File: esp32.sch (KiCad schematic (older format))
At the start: 41 parts, among them J1 Micro_SD_Card, J10 Conn_01x01, J11 Conn_01x04, J12 Conn_01x01, J13 Conn_01x01, J14 Conn_01x01, J15 Conn_01x01, J18 Conn_01x02, J2 Conn_01x06, J25 Conn_01x01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

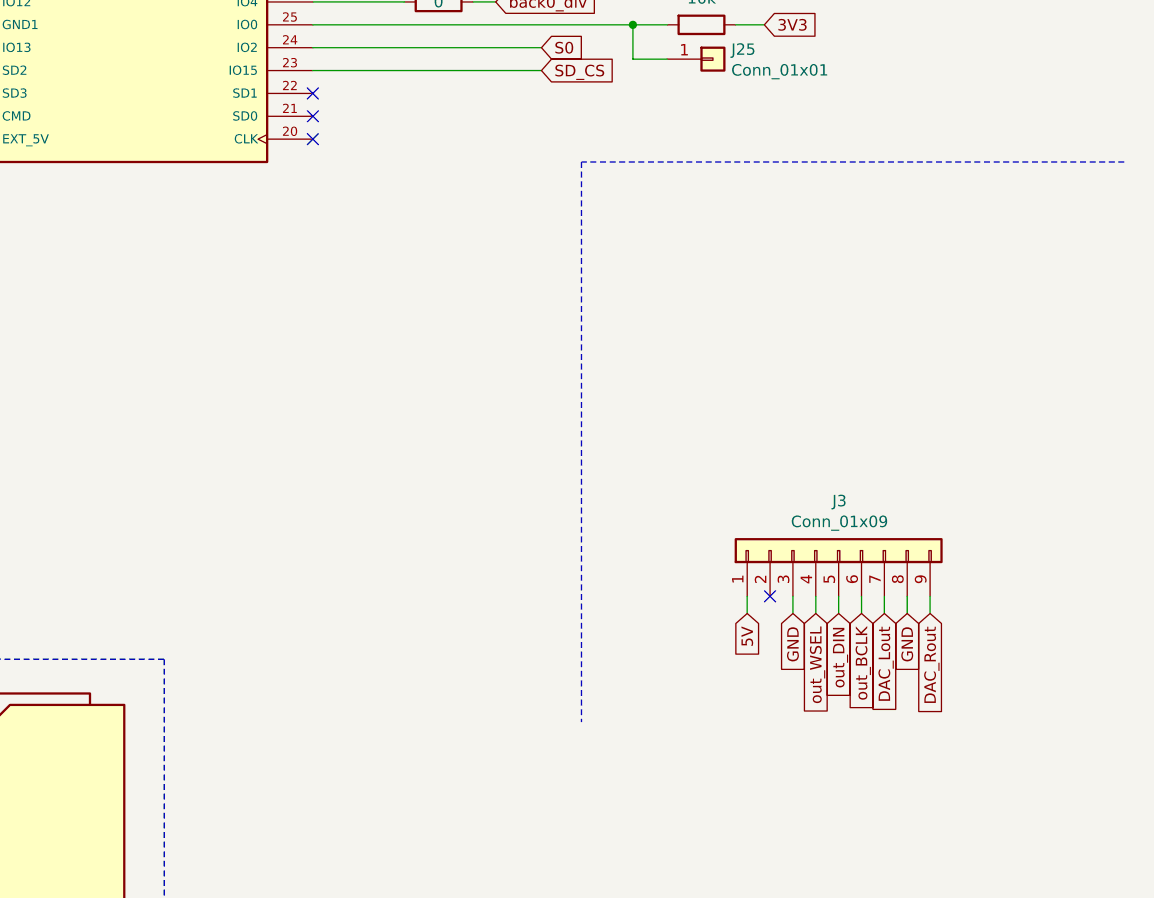
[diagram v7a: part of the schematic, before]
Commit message: UDA1334
utilisation symbole et empreinte compléte du module adafruit uda1334 à la place du simple connecteur
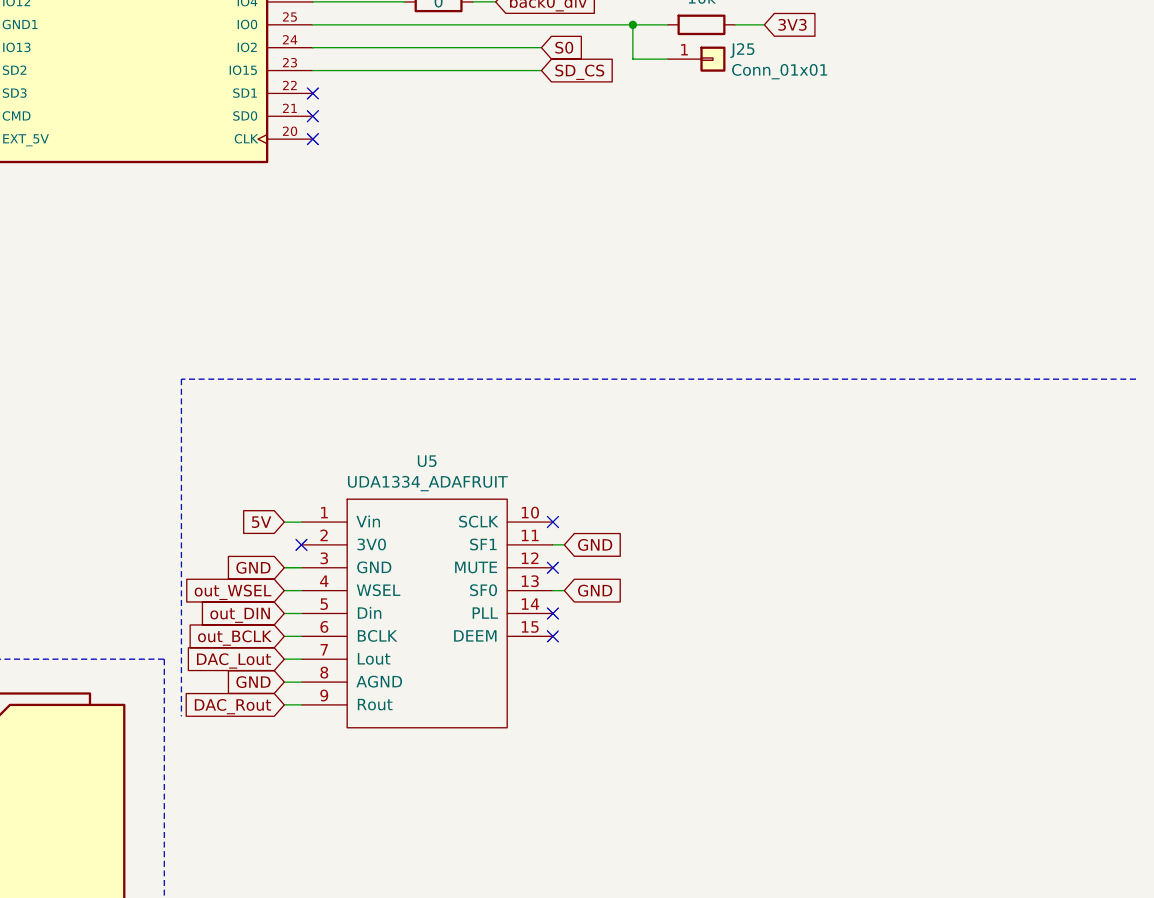
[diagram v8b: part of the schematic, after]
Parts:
- removed J3: Conn_01x09, Connector_PinSocket_2.54mm:PinSocket_1x09_P2.54mm_Vertical, symbol Connector_Generic:Conn_01x09
- added U5: UDA1334_ADAFRUIT, Chimere:Adafruit_UDA1334, symbol Chimere:UDA1334_ADAFRUIT
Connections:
- net 5V: now also U5.1 (Vin)
- net DAC_Lout: now also U5.7 (Lout)
- net DAC_Rout: now also U5.9 (Rout)
- net GND: now also U5.11 (SF1), U5.13 (SF0), U5.3 (GND), U5.8 (AGND)
- net out_BCLK: now also U5.6 (BCLK)
- net out_DIN: now also U5.5 (Din)
- net out_WSEL: now also U5.4 (WSEL)
- no-connect marks 12 -> 16
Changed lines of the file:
@@
 Wire Notes Line
 	500  1425 4975 1425
-Text GLabel 9800 6025 3    50   Input ~ 0
+Text GLabel 7475 5925 0    50   Input ~ 0
 out_WSEL
-Text GLabel 9900 6025 3    50   Input ~ 0
+Text GLabel 7475 6025 0    50   Input ~ 0
 out_DIN
-Text GLabel 10000 6025 3    50   Input ~ 0
+Text GLabel 7475 6125 0    50   Input ~ 0
 out_BCLK
 $Bitmap
-Pos 9950 4875
+Pos 10075 5775
 Scale 1.000000
 Data
@@
 EndData
 $EndBitmap
-Text GLabel 9700 6025 3    50   Input ~ 0
+Text GLabel 7475 5825 0    50   Input ~ 0
 GND
-Text GLabel 9500 6025 3    50   Input ~ 0
+Text GLabel 7475 5625 0    50   Input ~ 0
 5V
-$Comp
-L Connector_Generic:Conn_01x09 J3
-U 1 1 604855FC
-P 9900 5750
-F 0 "J3" V 10117 5746 50  0000 C CNN
-F 1 "Conn_01x09" V 10026 5746 50  0000 C CNN
-F 2 "Connector_PinSocket_2.54mm:PinSocket_1x09_P2.54mm_Vertical" H 9900 5750 50  0001 C CNN
-F 3 "~" H 9900 5750 50  0001 C CNN
-	1    9900 5750
-	0    -1   -1   0
-$EndComp
-NoConn ~ 9600 5950
-Text GLabel 10100 6025 3    50   Input ~ 0
+Text GLabel 7475 6225 0    50   Input ~ 0
 DAC_Lout
-Text GLabel 10300 6025 3    50   Input ~ 0
+Text GLabel 7475 6425 0    50   Input ~ 0
 DAC_Rout
-Text GLabel 10200 6025 3    50   Input ~ 0
+Text GLabel 7475 6325 0    50   Input ~ 0
 GND
-Wire Wire Line
-	9500 5950 9500 6025
-Wire Wire Line
-	9700 5950 9700 6025
-Wire Wire Line
-	9800 5950 9800 6025
-Wire Wire Line
-	9900 5950 9900 6025
-Wire Wire Line
-	10000 5950 10000 6025
-Wire Wire Line
-	10100 5950 10100 6025
-Wire Wire Line
-	10200 5950 10200 6025
-Wire Wire Line
-	10300 5950 10300 6025
-Wire Notes Line
-	11150 4050 8775 4050
-Wire Notes Line
-	8775 4050 8775 6500
 Text GLabel 5200 2450 0    50   Input ~ 0
 TILT
@@
 Wire Wire Line
 	5200 2950 6000 2950
+$Comp
+L Chimere:UDA1334_ADAFRUIT U5
+U 1 1 606CC25D
+P 8100 5925
+F 0 "U5" H 8100 6490 50  0000 C CNN
+F 1 "UDA1334_ADAFRUIT" H 8100 6399 50  0000 C CNN
+F 2 "Chimere:Adafruit_UDA1334" H 7950 5925 50  0001 C CNN
+F 3 "" H 7950 5925 50  0001 C CNN
+	1    8100 5925
+	1    0    0    -1
+$EndComp
+Wire Wire Line
+	7475 5625 7550 5625
+NoConn ~ 7550 5725
+Wire Wire Line
+	7475 5825 7550 5825
+Wire Wire Line
+	7475 5925 7550 5925
+Wire Wire Line
+	7475 6025 7550 6025
+Wire Wire Line
+	7475 6125 7550 6125
+Wire Wire Line
+	7475 6225 7550 6225
+Wire Wire Line
+	7475 6325 7550 6325
+Wire Wire Line
+	7475 6425 7550 6425
+NoConn ~ 8650 5625
+NoConn ~ 8650 5825
+NoConn ~ 8650 6025
+NoConn ~ 8650 6125
+Text GLabel 8700 5725 2    50   Input ~ 0
+GND
+Text GLabel 8700 5925 2    50   Input ~ 0
+GND
+Wire Wire Line
+	8650 5725 8700 5725
+Wire Wire Line
+	8650 5925 8700 5925
+Wire Notes Line
+	11200 5000 7025 5000
+Wire Notes Line
+	7025 5000 7025 6475
 $EndSCHEMATC
